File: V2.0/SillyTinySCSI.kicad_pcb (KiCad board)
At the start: 4 copper layers, 53.5 x 25 mm, 51 parts, among them J1 DB25_Plug, J2 Micro_SD_Card_Det1, U1 74LVT125, U2 74LVT245, U3 74LVT125, U4 74LVT245, U5 TLV75728PDBVR, U6 Pico W

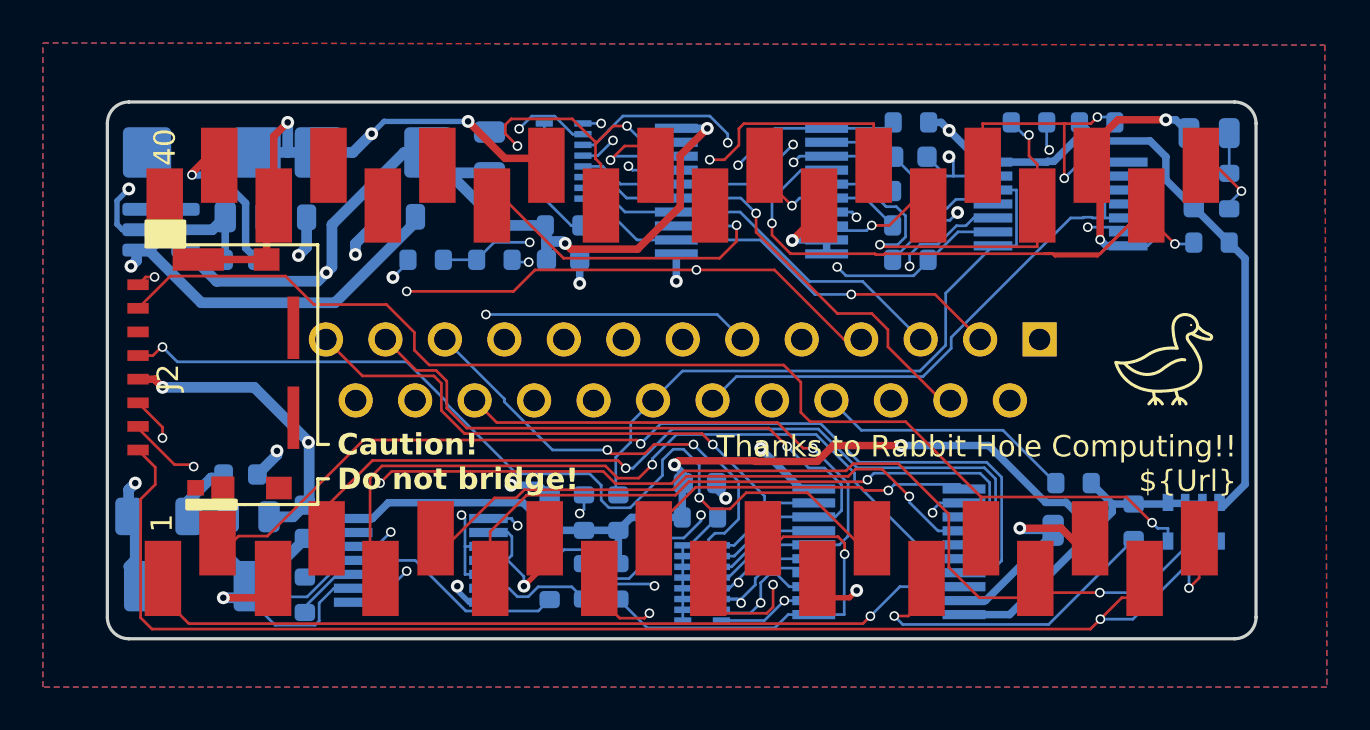
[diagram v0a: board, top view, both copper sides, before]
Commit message: fix second round of DRC, new prod
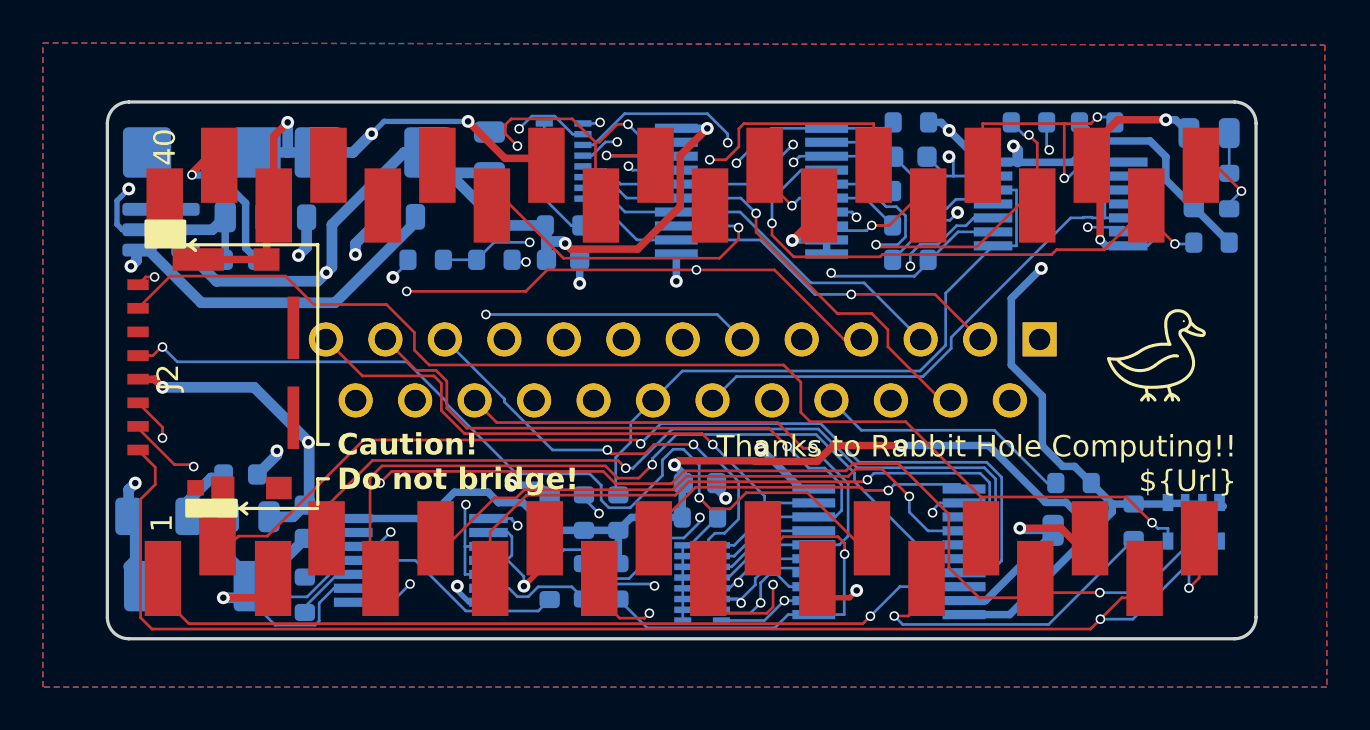
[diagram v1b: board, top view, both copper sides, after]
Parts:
- moved G*** 0.38 mm to (156.9, 62.0)
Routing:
- net +3V0: track 181.3 -> 188.5 mm, vias 8 -> 10
- net ~{DBGLOG}: track 31.9 -> 26.3 mm
- net ~{GPIO_CD_SEL}: track 19.9 -> 18.6 mm
- net ~{OUT_BSY}: track 40.0 -> 41.2 mm
- net ~{SCSI_RST}: track 50.9 -> 51.5 mm

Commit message: optimizations to buffers
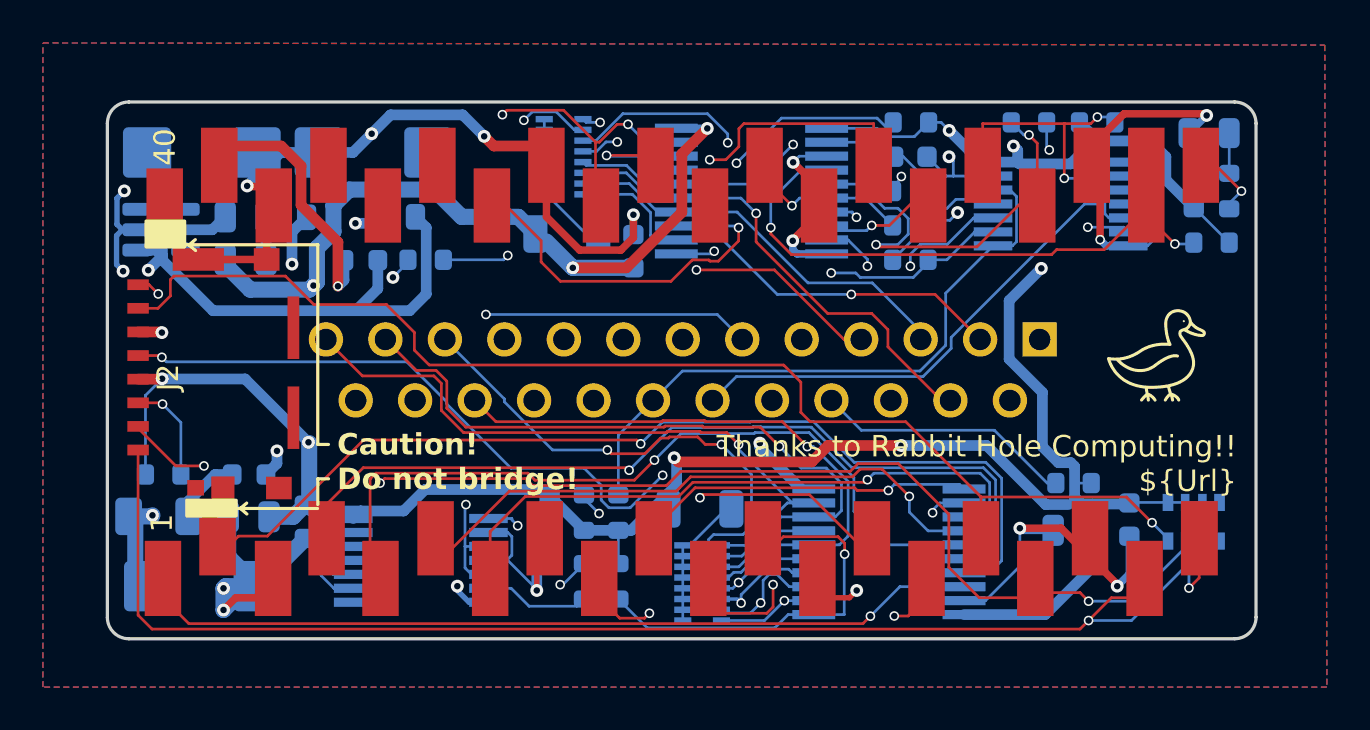
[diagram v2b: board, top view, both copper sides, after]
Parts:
- removed R14, R8: 4k7, Resistor_SMD:R_0603_1608Metric
- removed R3: 1k, Resistor_SMD:R_0603_1608Metric
- R10, R11: footprint Resistor_SMD:R_0603_1608Metric -> Resistor_SMD:R_1206_3216Metric
- moved R16 45.3 mm to (110.6, 67.6), turned to 180 degrees
- moved C4 20.1 mm to (155.6, 69.7), turned to -90 degrees
- moved C10 12.4 mm to (114.4, 57.6), turned to 0 degrees
- moved L2 5.61 mm to (119.8, 57.6), turned to 0 degrees
- moved C1 3.30 mm to (132.5, 57.2), turned to 90 degrees
- moved R11 0.44 mm to (129.4, 56.4)
- moved L1 0.40 mm to (114.6, 67.6)
- moved R10 0.40 mm to (135.6, 69.2)
- moved RN2 0.20 mm to (129.2, 52.8)
- turned C5 to -90 degrees
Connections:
- C1 pad 1: +3V0 -> +2V8
- C10 pad 1: +3V0 -> +2V8
- C11 pad 1: +3V0 -> +2V8
- C12 pad 2: +3V0 -> +2V8
- C13 pad 2: +3V0 -> +2V8
- C3 pad 1: +3V0 -> +2V8
- C4 pad 1: +3V0 -> +2V8
- C5 pad 1: +3V0 -> +2V8
- C6 pad 2: +3V0 -> +2V8
- D2 pad 2: +3V0 -> +2V8
- J2 pad 4: +3V0 -> +2V8
- R10 pad 1: +3V0 -> +2V8
- R11 pad 1: +3V0 -> +2V8
- R12 pad 2: +3V0 -> +2V8
- R13 pad 2: +3V0 -> +2V8
- R16 pad 2: +3V0 -> +2V8
- R17 pad 1: +3V0 -> +2V8
- R18 pad 1: +3V0 -> +2V8
- R6 pad 1: +3V0 -> +2V8
- R7 pad 1: +3V0 -> +2V8
- R9 pad 1: +3V0 -> +2V8
- RN3 pad 5: +3V0 -> +2V8
- RN3 pad 6: +3V0 -> +2V8
- RN3 pad 7: +3V0 -> +2V8
- RN3 pad 8: +3V0 -> +2V8
- U1 pad 10: ~{OUT_RST} -> GND
- U1 pad 11: ~{IN_RST} -> unconnected-(U1-Pad11)
- U1 pad 12: ~{SCSI_RST} -> GND
- U1 pad 14: +3V0 -> +2V8
- U1 pad 8: ~{SCSI_RST} -> unconnected-(U1-Pad8)
- U2 pad 1: ~{GPIO_ATN} -> +2V8
- U2 pad 11: GND -> ~{IN_RST}
- U2 pad 17: Net-(U2-B1) -> unconnected-(U2-B1-Pad17)
- U2 pad 20: +3V0 -> +2V8
- U2 pad 3: ~{SCSI_ACK} -> GND
- U2 pad 9: GND -> ~{SCSI_RST}
- U3 pad 14: +3V0 -> +2V8
- U4 pad 20: +3V0 -> +2V8
- U5 pad 5: +3V0 -> +2V8
- U6 pad 27: /cpu/GPIO_RST -> ~{IN_RST}
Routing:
- net +2V8: track 0.00 -> 196.4 mm, vias 0 -> 10
- net +3V0: track 188.5 -> 0.00 mm, vias 10 -> 0
- net /cpu/GPIO_RST: track 37.2 -> 0.00 mm, vias 2 -> 0
- net ~{SCSI_RST}: track 51.5 -> 24.5 mm, vias 5 -> 3
- net GND: track 112.6 -> 134.9 mm, vias 20 -> 22
- net Net-(U2-B1): track 9.47 -> 0.00 mm, vias 2 -> 0
- net /cpu/SDIO_CMD: track 55.3 -> 46.6 mm
- net +5V: track 41.0 -> 46.9 mm
- net ~{IN_RST}: track 10.3 -> 16.0 mm, vias 0 -> 2
- net Net-(U6-VSYS): track 7.79 -> 11.8 mm
- net /cpu/SDIO_CLK: track 43.1 -> 39.9 mm, vias 2 -> 3
- net ~{GPIO_MSG_BSY}: track 36.5 -> 38.7 mm
- net ~{OUT_RST}: track 2.14 -> 0.00 mm
- net ~{SCSI_DB7}: track 30.0 -> 31.9 mm
- net ~{SCSI_DB5}: track 26.8 -> 28.7 mm
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
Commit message: reverted some nuffer changes
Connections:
- U1 pad 11: unconnected-(U1-Pad11) -> ~{IN_RST}
- U1 pad 12: GND -> ~{SCSI_RST}
- U2 pad 11: ~{IN_RST} -> unconnected-(U2-B7-Pad11)
- U2 pad 9: ~{SCSI_RST} -> GND
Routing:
- net ~{IN_RST}: track 16.0 -> 47.8 mm
- net ~{SCSI_RST}: track 24.5 -> 45.9 mm, vias 3 -> 4
- net GND: track 134.9 -> 131.8 mm

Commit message: last resistor pack
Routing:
- net +2V8: track 196.4 -> 194.6 mm
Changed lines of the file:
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@@
   (segment (start 153.407781 53.8037) (end 152.5688 53.8037) (width 0.127) (layer "B.Cu") (net 22))
   (segment (start 154.676 50.951) (end 154.109994 50.951) (width 0.127) (layer "B.Cu") (net 22))
+  (segment (start 135.9422 51.4802) (end 134.757 52.6654) (width 0.5) (layer "F.Cu") (net 23))
   (segment (start 110.530004 63.16) (end 110.55 63.140004) (width 0.5) (layer "F.Cu") (net 23))
+  (segment (start 132.824989 57.975011) (end 130.85 57.975011) (width 0.5) (layer "F.Cu") (net 23))
   (segment (start 109.43 63.16) (end 110.530004 63.16) (width 0.5) (layer "F.Cu") (net 23))
+  (segment (start 134.757 56.043) (end 132.824989 57.975011) (width 0.5) (layer "F.Cu") (net 23))
   (segment (start 140.803643 67.015596) (end 134.596999 67.015596) (width 0.5) (layer "F.Cu") (net 23))
-  (segment (start 134.757 52.6654) (end 134.757 55.393) (width 0.5) (layer "F.Cu") (net 23))
+  (segment (start 134.757 52.6654) (end 134.757 56.043) (width 0.5) (layer "F.Cu") (net 23))
   (segment (start 144.98 66.25) (end 141.569239 66.25) (width 0.5) (layer "F.Cu") (net 23))
-  (segment (start 135.9422 51.4802) (end 134.757 52.6654) (width 0.5) (layer "F.Cu") (net 23))
-  (segment (start 132.174989 57.975011) (end 129.678511 57.975011) (width 0.5) (layer "F.Cu") (net 23))
-  (segment (start 134.757 55.393) (end 132.174989 57.975011) (width 0.5) (layer "F.Cu") (net 23))
   (segment (start 141.569239 66.25) (end 140.803643 67.015596) (width 0.5) (layer "F.Cu") (net 23))
   (segment (start 134.596999 67.015596) (end 134.399647 66.818244) (width 0.5) (layer "F.Cu") (net 23))
@@
   (via (at 135.9422 51.4802) (size 0.6) (drill 0.3) (layers "F.Cu" "B.Cu") (net 23))
   (via (at 117.600004 58.799996) (size 0.6) (drill 0.3) (layers "F.Cu" "B.Cu") (net 23))
-  (via (at 129.678511 57.975011) (size 0.6) (drill 0.3) (layers "F.Cu" "B.Cu") (net 23))
+  (via (at 130.85 57.975011) (size 0.6) (drill 0.3) (layers "F.Cu" "B.Cu") (net 23))
   (via (at 147.2076 51.5758) (size 0.6) (drill 0.3) (layers "F.Cu" "B.Cu") (net 23))
   (via (at 117.3665 66.1) (size 0.6) (drill 0.3) (layers "F.Cu" "B.Cu") (net 23))
@@
   (via (at 151.5 58) (size 0.6) (drill 0.3) (layers "F.Cu" "B.Cu") (net 23))
   (via (at 150.2 52.3) (size 0.6) (drill 0.3) (layers "F.Cu" "B.Cu") (net 23))
-  (segment (start 133.3 61.92705) (end 133.3 60.85) (width 0.5) (layer "In2.Cu") (net 23))
-  (segment (start 130.425011 57.975011) (end 129.678511 57.975011) (width 0.5) (layer "In2.Cu") (net 23))
-  (segment (start 134.650007 65.5) (end 134.650007 63.277057) (width 0.5) (layer "In2.Cu") (net 23))
-  (segment (start 134.399647 65.75036) (end 134.650007 65.5) (width 0.5) (layer "In2.Cu") (net 23))
+  (segment (start 134.399647 66.818244) (end 134.650007 66.567884) (width 0.5) (layer "In2.Cu") (net 23))
   (segment (start 116.72 59.68) (end 117.600004 58.799996) (width 0.75) (layer "In2.Cu") (net 23))
   (segment (start 116.72 65.4535) (end 116.72 59.68) (width 0.75) (layer "In2.Cu") (net 23))
   (segment (start 151.5 53.6) (end 150.2 52.3) (width 0.5) (layer "In2.Cu") (net 23))
   (segment (start 135.9422 51.4802) (end 136.0724 51.35) (width 0.5) (layer "In2.Cu") (net 23))
+  (segment (start 117.3665 66.1) (end 116.72 65.4535) (width 0.75) (layer "In2.Cu") (net 23))
+  (segment (start 133.3 61.92705) (end 133.3 60.425011) (width 0.5) (layer "In2.Cu") (net 23))
+  (segment (start 133.3 60.425011) (end 130.85 57.975011) (width 0.5) (layer "In2.Cu") (net 23))
+  (segment (start 146.9542 51.3224) (end 147.2076 51.5758) (width 0.35) (layer "In2.Cu") (net 23))
   (segment (start 134.650007 63.277057) (end 133.3 61.92705) (width 0.5) (layer "In2.Cu") (net 23))
-  (segment (start 117.3665 66.1) (end 116.72 65.4535) (width 0.75) (layer "In2.Cu") (net 23))
-  (segment (start 134.399647 66.818244) (end 134.399647 65.75036) (width 0.5) (layer "In2.Cu") (net 23))
-  (segment (start 146.9542 51.3224) (end 147.2076 51.5758) (width 0.35) (layer "In2.Cu") (net 23))
-  (segment (start 133.3 60.85) (end 130.425011 57.975011) (width 0.5) (layer "In2.Cu") (net 23))
   (segment (start 151.5 58) (end 151.5 53.6) (width 0.5) (layer "In2.Cu") (net 23))
+  (segment (start 134.650007 66.567884) (end 134.650007 63.277057) (width 0.5) (layer "In2.Cu") (net 23))
   (segment (start 135.9422 51.4802) (end 136.1 51.3224) (width 0.35) (layer "In2.Cu") (net 23))
   (segment (start 136.0724 51.35) (end 146.9818 51.35) (width 0.5) (layer "In2.Cu") (net 23))

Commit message: before ar
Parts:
- removed RN1, RN2: 100, Resistor_SMD:R_Array_Convex_8x0602
- added C14: 10uF, Capacitor_SMD:C_0805_2012Metric, B.Cu at (130.4, 72.8)
- added C15: 10uF, Capacitor_SMD:C_0805_2012Metric, B.Cu at (125.5, 52.2)
- added R14: 110, Resistor_SMD:R_0603_1608Metric, B.Cu at (128.2, 51.5)
- added R21: 110, Resistor_SMD:R_0603_1608Metric, B.Cu at (131.2, 51.5)
- added R22: 110, Resistor_SMD:R_0603_1608Metric, B.Cu at (128.2, 53.1)
- added R23: 110, Resistor_SMD:R_0603_1608Metric, B.Cu at (131.2, 53.1)
- added R24: 110, Resistor_SMD:R_0603_1608Metric, B.Cu at (135.1, 73.7)
- added R25: 110, Resistor_SMD:R_0603_1608Metric, B.Cu at (138.1, 73.7)
- added R26: 110, Resistor_SMD:R_0603_1608Metric, B.Cu at (135.1, 72.1)
- added R27: 110, Resistor_SMD:R_0603_1608Metric, B.Cu at (138.1, 72.1)
- added R28: 110, Resistor_SMD:R_0603_1608Metric, B.Cu at (135.1, 70.5)
- added R29: 110, Resistor_SMD:R_0603_1608Metric, B.Cu at (138.1, 70.5)
- added R3: 110, Resistor_SMD:R_0603_1608Metric, B.Cu at (128.2, 56.3)
- added R30: 110, Resistor_SMD:R_0603_1608Metric, B.Cu at (135.1, 68.9)
- added R31: 110, Resistor_SMD:R_0603_1608Metric, B.Cu at (138.1, 68.9)
- added R8: 110, Resistor_SMD:R_0603_1608Metric, B.Cu at (131.2, 56.3)
- R10, R11: value 10 -> 110; footprint Resistor_SMD:R_1206_3216Metric -> Resistor_SMD:R_0603_1608Metric
- moved R10 16.3 mm to (128.2, 54.7), turned to 180 degrees
- moved R11 2.49 mm to (131.2, 54.7), turned to 180 degrees
- moved R1 1.62 mm to (128.6, 72.8)
- moved C1 1.06 mm to (131.8, 58.0), turned to 0 degrees
- moved R6 0.58 mm to (132.2, 73.0)
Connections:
- R10 pad 1: +2V8 -> ~{SCSI_CD}
- R10 pad 2: Net-(RN1-R1.2) -> +2V8
- R11 pad 1: +2V8 -> ~{SCSI_REQ}
- R11 pad 2: Net-(RN2-R1.2) -> +2V8
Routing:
- net ~{IN_RST}: track 47.8 -> 0.00 mm, vias 2 -> 0
- net ~{SCSI_DB5}: track 28.7 -> 2.09 mm, vias 2 -> 0
- net +2V8: track 194.6 -> 220.0 mm
- net ~{GPIO_DBP}: track 27.5 -> 3.56 mm, vias 2 -> 0
- net ~{SCSI_DB3}: track 22.5 -> 2.21 mm, vias 1 -> 0
- net ~{SCSI_DB1}: track 19.0 -> 2.34 mm, vias 1 -> 0
- net ~{SCSI_SEL}: track 41.6 -> 25.6 mm, vias 1 -> 0
- net ~{SCSI_DB2}: track 19.8 -> 5.50 mm, vias 1 -> 0
- net ~{SCSI_DB0}: track 20.1 -> 5.79 mm, vias 1 -> 0
- net ~{SCSI_BSY}: track 39.7 -> 26.7 mm, vias 3 -> 2
- net ~{SCSI_ACK}: track 26.2 -> 13.9 mm, vias 2 -> 1
- net GND: track 131.8 -> 121.6 mm, vias 22 -> 21
- net ~{SCSI_RST}: track 45.9 -> 36.6 mm, vias 4 -> 2
- net Net-(RN2-R1.2): track 6.58 -> 0.00 mm
- net Net-(RN1-R1.2): track 5.90 -> 0.00 mm
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
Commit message: before ar2
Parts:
- moved C1 4.00 mm to (127.8, 57.9), turned to 180 degrees
- moved R24 0.60 mm to (134.5, 73.7)
- moved R26 0.60 mm to (134.5, 72.1)
- moved R28 0.60 mm to (134.5, 70.5)
- moved R30 0.60 mm to (134.5, 68.9)
- moved R10 0.42 mm to (127.8, 54.7)
- moved R14 0.42 mm to (127.8, 51.5)
- moved R3 0.42 mm to (127.8, 56.3)
- moved R22 0.42 mm to (127.8, 53.1)
- moved C15 0.20 mm to (125.3, 52.2)
- moved D2 0.20 mm to (123.8, 55.6)
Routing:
- net ~{IN_RST}: track 0.00 -> 48.0 mm, vias 0 -> 2
- net ~{SCSI_DB4}: track 28.6 -> 0.00 mm, vias 1 -> 0
- net +2V8: track 220.0 -> 197.9 mm
- net ~{GPIO_ACK}: track 15.7 -> 0.00 mm, vias 2 -> 0
- net ~{SCSI_RST}: track 36.6 -> 49.9 mm, vias 2 -> 4
- net ~{DATA_DIR}: track 37.5 -> 28.3 mm
- net ~{SCSI_DB0}: track 5.79 -> 0.00 mm
- net ~{SCSI_DB2}: track 5.50 -> 0.00 mm
- net ~{SCSI_DB6}: track 32.7 -> 27.4 mm
- net ~{GPIO_DB2}: track 38.8 -> 42.4 mm
- net ~{SCSI_DB7}: track 28.6 -> 25.8 mm
- net ~{SCSI_DB1}: track 2.34 -> 0.00 mm
- net ~{SCSI_DB3}: track 2.21 -> 0.00 mm
- net ~{SCSI_DB5}: track 2.09 -> 0.00 mm
- net GND: track 121.6 -> 120.2 mm
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
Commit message: ar2, re-route
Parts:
- moved R1 0.20 mm to (128.6, 73.0)
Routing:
- net ~{SCSI_DB0}: track 0.00 -> 54.8 mm, vias 0 -> 4
- net ~{SCSI_DB1}: track 0.00 -> 42.9 mm, vias 0 -> 2
- net +2V8: track 197.9 -> 228.5 mm
- net ~{SCSI_DB3}: track 0.00 -> 30.0 mm, vias 0 -> 2
- net ~{SCSI_DB4}: track 0.00 -> 28.5 mm, vias 0 -> 2
- net ~{SCSI_DB5}: track 0.00 -> 25.7 mm, vias 0 -> 2
- net ~{DATA_DIR}: track 28.3 -> 50.3 mm, vias 2 -> 3
- net ~{SCSI_DB2}: track 0.00 -> 21.2 mm, vias 0 -> 2
- net ~{SCSI_SEL}: track 25.6 -> 41.8 mm, vias 0 -> 1
- net ~{GPIO_ACK}: track 0.00 -> 15.7 mm, vias 0 -> 2
- net ~{SCSI_ACK}: track 14.0 -> 24.9 mm, vias 1 -> 2
- net ~{SCSI_MSG}: track 16.1 -> 26.1 mm
- net ~{SCSI_CD}: track 17.2 -> 26.6 mm, vias 1 -> 3
- net ~{SCSI_BSY}: track 27.5 -> 35.9 mm, vias 2 -> 3
- net ~{SCSI_DB6}: track 27.4 -> 33.0 mm, vias 1 -> 2
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
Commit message: ar3 all but pwr
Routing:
- net +2V8: track 228.5 -> 41.0 mm, vias 10 -> 2
- net GND: track 120.2 -> 41.9 mm, vias 21 -> 3
- net /cpu/SDIO_D2: track 62.5 -> 0.00 mm, vias 1 -> 0
- net /cpu/SDIO_D1: track 60.3 -> 0.00 mm, vias 3 -> 0
- net /cpu/SDIO_D3: track 58.5 -> 0.00 mm, vias 2 -> 0
- net /cpu/SDIO_D0: track 58.3 -> 0.00 mm, vias 1 -> 0
- net ~{SCSI_DB0}: track 54.8 -> 0.00 mm, vias 4 -> 0
- net ~{DATA_DIR}: track 50.3 -> 0.00 mm, vias 3 -> 0
- net ~{SCSI_RST}: track 50.3 -> 0.00 mm, vias 4 -> 0
- net ~{IN_RST}: track 48.2 -> 0.00 mm, vias 2 -> 0
- net /cpu/SDIO_CMD: track 46.6 -> 0.00 mm, vias 2 -> 0
- net ~{GPIO_DB1}: track 46.3 -> 1.39 mm, vias 1 -> 0
- net ~{OUT_BSY}: track 42.1 -> 0.00 mm, vias 4 -> 0
- net ~{SCSI_SEL}: track 41.8 -> 0.00 mm, vias 1 -> 0
- net ~{GPIO_DB2}: track 42.4 -> 2.46 mm, vias 1 -> 0
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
